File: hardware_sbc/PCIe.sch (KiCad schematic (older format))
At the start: 23 parts, among them J5 Bus_PCI_Express_Mini, U1 IMX8MM, U13 MIC94164

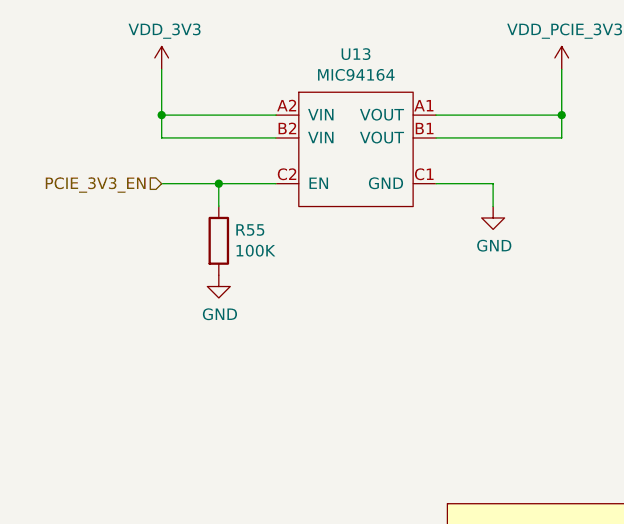
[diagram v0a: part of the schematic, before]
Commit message: DNP PCIE_3V3_EN pull-down
This part has an internal 2M pulldown, so this is no needed, but
could be useful for rework (if we want to use a different signal
to turn this on, for example). Move things around a bit to make this
possible.
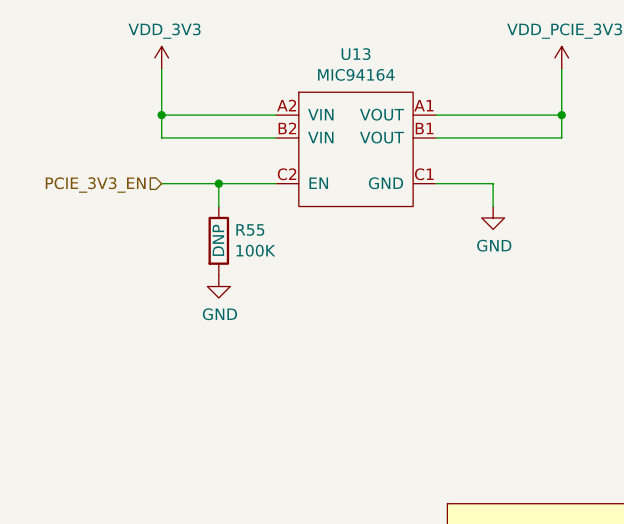
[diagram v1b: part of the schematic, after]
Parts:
- R55: Populate (none) -> DNP
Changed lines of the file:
@@
 F 6 "311-100KNCT-ND" H 1650 2300 50  0001 C CNN "Vendorpart"
 F 7 "RC0201JR-07100KL" H 1650 2300 50  0001 C CNN "Mfgrpart"
+F 8 "DNP" V 1650 2300 50  0000 C CNN "Populate"
 	1    1650 2300
 	1    0    0    -1

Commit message: Change mPCIe connector to taller 2041262-1
Fixes #7
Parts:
- J5: Mfgrpart 1775838-2 -> 2041262-1; Vendorpart A123340CT-ND -> A125147CT-ND
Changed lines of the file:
@@
 F 4 "TE" H 7350 3750 50  0001 C CNN "Mfgr"
 F 5 "" H 7350 3750 50  0001 C CNN "Part"
-F 6 "A123340CT-ND" H 7350 3750 50  0001 C CNN "Vendorpart"
-F 7 "1775838-2" H 7350 3750 50  0001 C CNN "Mfgrpart"
+F 6 "A125147CT-ND" H 7350 3750 50  0001 C CNN "Vendorpart"
+F 7 "2041262-1 " H 7350 3750 50  0001 C CNN "Mfgrpart"
 	1    7350 3750
 	1    0    0    1
